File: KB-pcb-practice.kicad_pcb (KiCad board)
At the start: 2 copper layers, 435 parts, among them J1 Conn_01x03, SW1 Reset, SW10 F7, SW100 R_CTRL, SW101 L_ARROW, SW102 DN_ARROW, SW103 R_ARROW, SW104 PAD_0, SW105 PAD_., SW106 PAD_ENTER, SW11 F8, SW12 F9, SW13 F10, SW14 F11, SW15 F12, SW16 PRT_SC, SW17 SCR_LK, SW18 PAUSE, SW19 TILDE, SW2 Boot, SW20 1, SW21 2, SW22 3, SW23 4, SW24 5, SW25 6, SW26 7, SW27 8, SW28 9, SW29 0, SW3 ESC, SW30 -, SW31 =, SW32 BACKSPACE, SW33 INSERT, SW34 HOME, SW35 PG_UP, SW36 NUM_LK, SW37 PAD_/, SW38 *, SW39 PAD_-, SW4 F1, SW40 TAB, SW41 Q, SW42 W, SW43 E, SW44 R, SW45 T, SW46 Y, SW47 U, SW48 I, SW49 O, SW5 F2, SW50 P, SW51 [, SW52 ], SW53 \, SW54 DEL, SW55 END, SW56 PG_DN, SW57 PAD_7, SW58 PAD_8, SW59 PAD_9, SW6 F3, SW60 +, SW61 CAPS, SW62 A, SW63 S, SW64 D, SW65 F, SW66 G, SW67 H, SW68 J, SW69 K, SW7 F4, SW70 L, SW71 ;, SW72 ', SW73 ENTER, SW74 PAD_4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

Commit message: Routing Finished
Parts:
- moved R5 152.6 mm to (221.0, 198.6), turned to 90 degrees
- moved R4 149.3 mm to (223.0, 199.8), turned to 90 degrees
- moved U2 148.1 mm to (225.9, 206.9)
- moved C26 147.3 mm to (235.7, 206.0), turned to 90 degrees
- moved R7 147.2 mm to (223.0, 196.0), turned to -90 degrees
- moved C20 146.0 mm to (232.3, 201.2)
- moved C22 146.0 mm to (232.3, 199.0)
- moved C24 146.0 mm to (233.4, 196.0)
- moved C25 146.0 mm to (231.3, 196.0)
- moved R6 145.4 mm to (228.1, 195.3), turned to 0 degrees
- moved C27 143.2 mm to (237.7, 206.0), turned to 90 degrees
- moved R3 142.5 mm to (230.6, 190.4), turned to 0 degrees
- moved C18 140.9 mm to (230.6, 192.5), turned to 0 degrees
- moved D59 25.6 mm to (499.1, 141.2), turned to -90 degrees
- moved R_R17 22.5 mm to (416.1, 186.4), turned to -90 degrees
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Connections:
- R_B1 pad 1: CS1 -> CS7
- R_B10 pad 1: CS28 -> CS4
- R_B2 pad 1: CS4 -> CS10
- R_B3 pad 1: CS7 -> CS13
- R_B4 pad 1: CS10 -> CS16
- R_B5 pad 1: CS13 -> CS19
- R_B6 pad 1: CS16 -> CS22
- R_B7 pad 1: CS19 -> CS25
- R_B8 pad 1: CS22 -> CS28
- R_B9 pad 1: CS25 -> CS1
- R_G1 pad 1: CS3 -> CS9
- R_G10 pad 1: CS30 -> CS6
- R_G2 pad 1: CS6 -> CS12
- R_G3 pad 1: CS9 -> CS15
- R_G4 pad 1: CS12 -> CS18
- R_G5 pad 1: CS15 -> CS21
- R_G6 pad 1: CS18 -> CS24
- R_G7 pad 1: CS21 -> CS27
- R_G8 pad 1: CS24 -> CS30
- R_G9 pad 1: CS27 -> CS3
- R_R1 pad 1: CS2 -> CS8
- R_R10 pad 1: CS29 -> CS5
- R_R2 pad 1: CS5 -> CS11
- R_R3 pad 1: CS8 -> CS14
- R_R4 pad 1: CS11 -> CS17
- R_R5 pad 1: CS14 -> CS20
- R_R6 pad 1: CS17 -> CS23
- R_R7 pad 1: CS20 -> CS26
- R_R8 pad 1: CS23 -> CS29
- R_R9 pad 1: CS26 -> CS2
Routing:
- net SW4: track 0.00 -> 264.7 mm, vias 0 -> 11
- net SW10: track 13.7 -> 237.8 mm, vias 0 -> 7
- net SW9: track 24.5 -> 229.9 mm, vias 1 -> 10
- net CS40: track 11.9 -> 213.0 mm
- net CS42: track 0.00 -> 195.7 mm
- net CS41: track 0.00 -> 194.7 mm
- net +5V: track 232.4 -> 418.6 mm, vias 8 -> 10
- net CS43: track 0.00 -> 185.5 mm
- net Net-(LED57-R): track 0.00 -> 183.2 mm, vias 0 -> 10
- net Net-(LED55-R): track 0.00 -> 182.9 mm, vias 0 -> 10
- net Net-(LED100-R): track 0.00 -> 181.3 mm, vias 0 -> 10
- net Net-(LED13-R): track 0.00 -> 168.9 mm, vias 0 -> 10
- net SDA: track 191.2 -> 356.7 mm
- net Net-(LED18-R): track 0.09 -> 164.9 mm, vias 0 -> 10
- net Net-(LED16-R): track 0.00 -> 164.8 mm, vias 0 -> 10
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
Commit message: Revising for underglow and PD IC
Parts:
- removed C16: 1u, Capacitor_SMD:C_0805_2012Metric_Pad1.18x1.45mm_HandSolder
- moved C15 51.6 mm to (378.8, 175.1)
- moved C17 51.6 mm to (376.7, 175.1)
- moved C19 51.6 mm to (371.7, 162.5)
- moved C21 51.6 mm to (372.7, 168.0), turned to 180 degrees
- moved C23 51.6 mm to (372.7, 165.7), turned to 180 degrees
- moved C29 51.6 mm to (360.6, 160.6)
- moved R10 51.6 mm to (361.2, 168.6)
- moved R11 51.6 mm to (359.2, 167.3)
- moved R12 51.6 mm to (368.8, 163.5)
- moved R13 51.6 mm to (361.2, 164.8)
- moved R9 51.6 mm to (362.7, 160.6)
- moved U4 51.6 mm to (369.3, 173.9)
- moved R_B15 27.5 mm to (381.4, 185.3)
- moved R_R17 23.0 mm to (421.3, 208.8), turned to 180 degrees
- moved R_R14 22.4 mm to (353.6, 185.9), turned to -90 degrees
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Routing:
- net CS40: track 213.0 -> 13.4 mm
- net CS41: track 194.7 -> 12.7 mm
- net Net-(LED103-R): track 178.2 -> 0.00 mm, vias 6 -> 0
- net CS42: track 195.7 -> 18.8 mm
- net Net-(LED102-R): track 146.7 -> 0.00 mm, vias 8 -> 0
- net Net-(LED101-R): track 141.5 -> 0.00 mm, vias 6 -> 0
- net Net-(LED103-G): track 141.1 -> 0.00 mm
- net Net-(LED101-B): track 138.8 -> 0.00 mm
- net SDB: track 372.0 -> 233.9 mm, vias 4 -> 3
- net CS7: track 151.9 -> 18.8 mm
- net Net-(LED102-B): track 132.2 -> 0.00 mm
- net Net-(LED103-B): track 131.2 -> 0.00 mm
- net COL16: track 277.0 -> 146.2 mm
- net Net-(LED102-G): track 130.1 -> 0.00 mm
- net Net-(LED101-G): track 129.0 -> 0.00 mm
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
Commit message: Rearranged LED Drivers
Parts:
- removed C18: 0.1u, Capacitor_SMD:C_0805_2012Metric_Pad1.18x1.45mm_HandSolder
- removed R3, R4: 100k, Resistor_SMD:R_0805_2012Metric_Pad1.20x1.40mm_HandSolder
- removed R5, R7: 1k, Resistor_SMD:R_0805_2012Metric_Pad1.20x1.40mm_HandSolder
- added C16: 1u, Capacitor_SMD:C_0805_2012Metric_Pad1.18x1.45mm_HandSolder, B.Cu at (374.1, 162.6)
- moved C20 46.7 mm to (185.7, 202.6)
- moved C22 46.7 mm to (185.7, 200.4)
- moved C24 46.7 mm to (186.8, 197.4)
- moved C25 46.7 mm to (184.6, 197.4)
- moved U2 46.3 mm to (179.6, 207.4)
- moved R6 45.8 mm to (182.4, 197.4), turned to 90 degrees
- moved C26 45.7 mm to (190.0, 206.8)
- moved C27 45.6 mm to (192.2, 206.8)
- moved R_R16 37.9 mm to (398.9, 170.6), turned to 90 degrees
- moved R_G16 36.7 mm to (393.8, 170.5), turned to 90 degrees
- moved R_B16 35.2 mm to (391.3, 175.3)
- moved R_G17 23.2 mm to (418.1, 183.8), turned to 0 degrees
- moved R_R17 23.0 mm to (419.1, 185.9), turned to 0 degrees
- moved R_G15 18.1 mm to (379.6, 188.5), turned to 0 degrees
- moved R_B17 17.0 mm to (408.7, 179.1), turned to 90 degrees
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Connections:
- D101 pad 1: ROW5 -> ROW4
- D34 pad 1: ROW1 -> ROW2
- D54 pad 1: ROW2 -> ROW3
- D55 pad 1: ROW2 -> ROW4
- D88 pad 1: ROW4 -> ROW3
- R_B1 pad 1: CS7 -> CS13
- R_B10 pad 1: CS4 -> CS10
- R_B11 pad 1: CS40 -> CS49
- R_B12 pad 1: CS43 -> CS52
- R_B13 pad 1: CS46 -> CS55
- R_B14 pad 1: CS49 -> CS58
- R_B15 pad 1: CS52 -> CS31
- R_B16 pad 1: CS55 -> CS34
- R_B17 pad 1: CS58 -> CS37
- R_B18 pad 1: CS31 -> CS40
- R_B19 pad 1: CS34 -> CS43
- R_B2 pad 1: CS10 -> CS16
- R_B20 pad 1: CS39 -> CS48
- R_B3 pad 1: CS13 -> CS19
- R_B4 pad 1: CS16 -> CS22
- R_B5 pad 1: CS19 -> CS25
- R_B6 pad 1: CS22 -> CS28
- R_B7 pad 1: CS25 -> CS1
- R_B8 pad 1: CS28 -> CS4
- R_B9 pad 1: CS1 -> CS7
- R_G1 pad 1: CS9 -> CS15
- R_G10 pad 1: CS6 -> CS12
- R_G11 pad 1: CS42 -> CS51
- R_G12 pad 1: CS45 -> CS54
- R_G13 pad 1: CS48 -> CS57
- R_G14 pad 1: CS51 -> CS60
- R_G15 pad 1: CS54 -> CS32
- R_G16 pad 1: CS57 -> CS35
- R_G17 pad 1: CS60 -> CS38
- R_G18 pad 1: CS33 -> CS42
- R_G19 pad 1: CS36 -> CS45
- R_G2 pad 1: CS12 -> CS18
- R_G20 pad 1: CS38 -> CS47
- R_G3 pad 1: CS15 -> CS21
- R_G4 pad 1: CS18 -> CS24
- R_G5 pad 1: CS21 -> CS27
- R_G6 pad 1: CS24 -> CS30
- R_G7 pad 1: CS27 -> CS3
- R_G8 pad 1: CS30 -> CS6
- R_G9 pad 1: CS3 -> CS9
- R_R1 pad 1: CS8 -> CS14
- R_R10 pad 1: CS5 -> CS11
- R_R11 pad 1: CS41 -> CS50
- R_R12 pad 1: CS44 -> CS53
- R_R13 pad 1: CS47 -> CS56
- R_R14 pad 1: CS50 -> CS59
- R_R15 pad 1: CS53 -> CS33
- R_R16 pad 1: CS56 -> CS36
- R_R17 pad 1: CS59 -> CS39
- R_R18 pad 1: CS32 -> CS41
- R_R19 pad 1: CS35 -> CS44
- R_R2 pad 1: CS11 -> CS17
- R_R20 pad 1: CS37 -> CS46
- R_R3 pad 1: CS14 -> CS20
- R_R4 pad 1: CS17 -> CS23
- R_R5 pad 1: CS20 -> CS26
- R_R6 pad 1: CS23 -> CS29
- R_R7 pad 1: CS26 -> CS2
- R_R8 pad 1: CS29 -> CS5
- R_R9 pad 1: CS2 -> CS8
- SW102 pad 2: COL15 -> COL14
- SW103 pad 2: COL16 -> COL15
- SW104 pad 2: COL17 -> COL16
- SW105 pad 2: COL18 -> COL17
- SW106 pad 2: COL19 -> COL18
- SW35 pad 2: COL16 -> COL15
- SW36 pad 2: COL17 -> COL16
- SW37 pad 2: COL18 -> COL17
- SW38 pad 2: COL18 -> COL17
- SW39 pad 2: COL19 -> COL18
- SW56 pad 2: COL16 -> COL15
- SW57 pad 2: COL17 -> COL16
- SW58 pad 2: COL18 -> COL17
- SW59 pad 2: COL19 -> COL18
- SW60 pad 2: COL19 -> COL18
- SW74 pad 2: COL17 -> COL16
- SW75 pad 2: COL18 -> COL17
- SW76 pad 2: COL19 -> COL18
- SW89 pad 2: COL15 -> COL14
- SW90 pad 2: COL17 -> COL16
- SW91 pad 2: COL18 -> COL17
- SW92 pad 2: COL19 -> COL18
- U1 pad 15: COL19 -> RGB_DI
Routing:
- net INTB: track 228.0 -> 441.7 mm, vias 2 -> 4
- net SDB: track 233.9 -> 438.2 mm, vias 3 -> 4
- net SDA: track 238.9 -> 427.6 mm, vias 3 -> 4
- net +5V: track 324.1 -> 506.0 mm, vias 8 -> 6
- net SCL: track 250.8 -> 432.0 mm, vias 3 -> 4
- net COL14: track 119.6 -> 290.3 mm, vias 0 -> 2
- net COL15: track 102.6 -> 256.7 mm, vias 0 -> 2
- net COL19: track 152.7 -> 0.00 mm
- net Net-(LED102-R): track 0.00 -> 144.4 mm, vias 0 -> 8
- net Net-(LED101-R): track 0.00 -> 144.4 mm, vias 0 -> 6
- net Net-(LED103-R): track 0.00 -> 136.0 mm, vias 0 -> 6
- net Net-(LED102-G): track 0.00 -> 131.7 mm
- net Net-(LED101-G): track 0.00 -> 130.5 mm
- net Net-(LED101-B): track 0.00 -> 126.8 mm
- net Net-(LED102-B): track 0.00 -> 124.4 mm
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- added copper zone on B.Cu, net GND

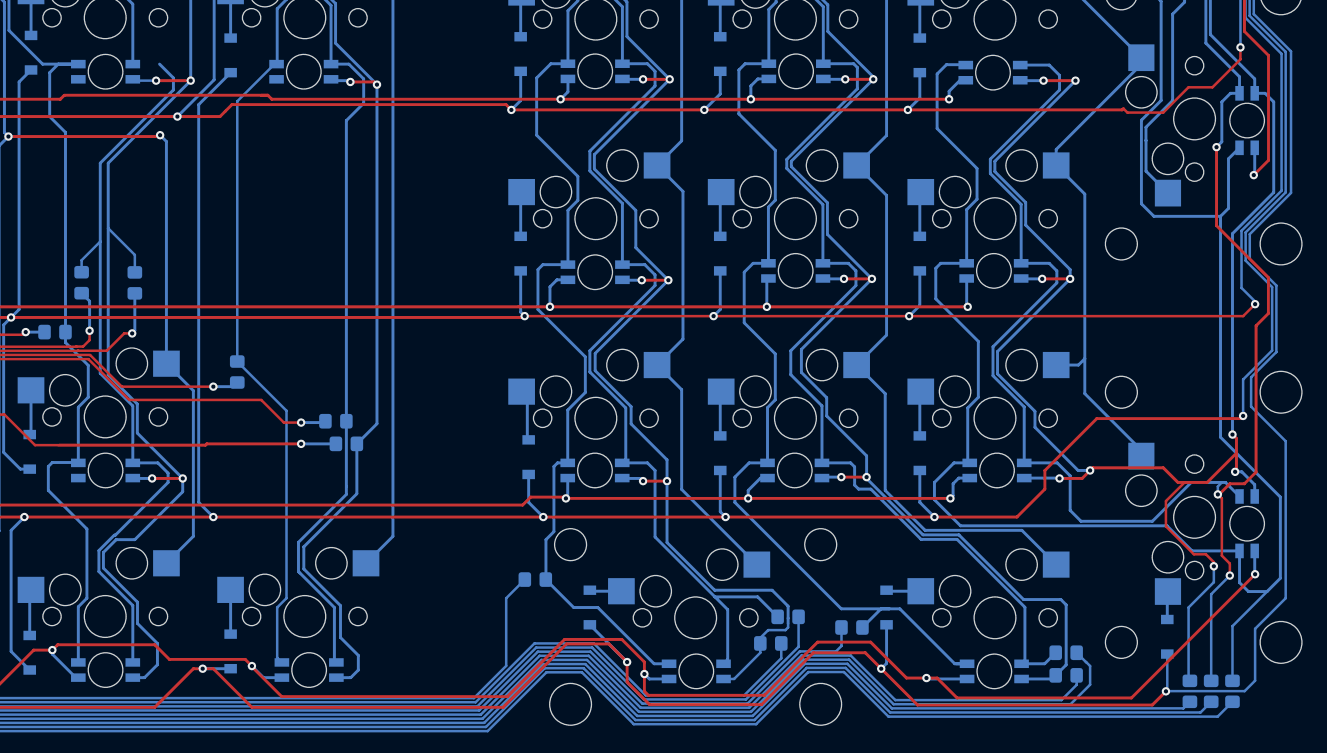
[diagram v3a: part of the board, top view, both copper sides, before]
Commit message: Fixed Majority of Errors in ERC
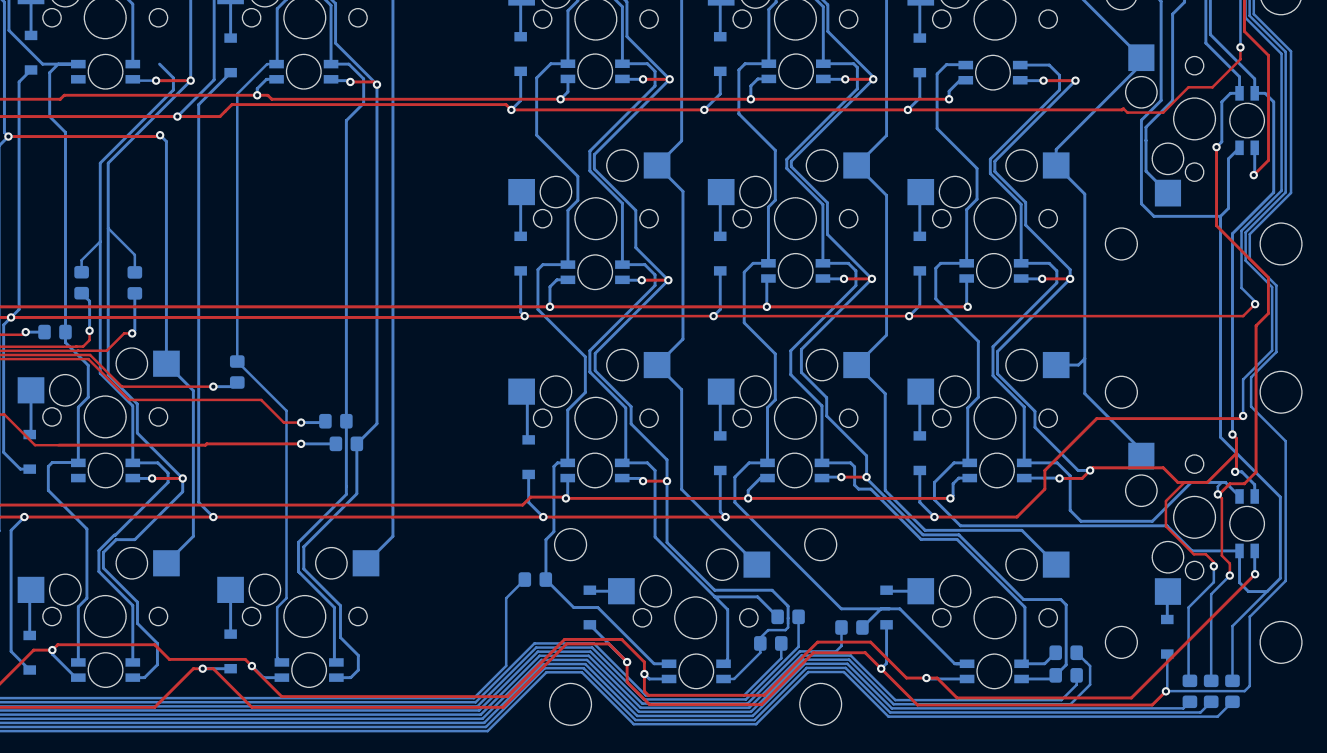
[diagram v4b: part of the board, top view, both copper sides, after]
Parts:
- F1: value 2.5 -> 3
- Y1: value ABLS-12.000MHZ-B4-T -> XTAL_ABLS_ABR
- renumbered R13 to R10, R10 to R7
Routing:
- net SW9: track 252.4 -> 254.6 mm, vias 8 -> 9
